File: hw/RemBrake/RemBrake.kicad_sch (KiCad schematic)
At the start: 5 parts, among them J1 Screw_Terminal_01x02, J2 Conn_01x03_MountingPin, J3 Screw_Terminal_01x04

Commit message: schematics update
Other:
- sheet brake_control ports: added none; removed RUNNIG (RED)
- sheet power_switch ports: added RUNNIG (RED); removed none
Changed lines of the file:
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@@
-	(wire
-		(pts
-			(xy 184.15 127) (xy 187.96 127)
-		)
-		(stroke
-			(width 0)
-			(type default)
-		)
-	)
 	(wire
 		(pts
@@
 	(wire
 		(pts
-			(xy 177.8 106.68) (xy 184.15 106.68)
+			(xy 205.74 76.2) (xy 205.74 95.25)
 		)
 		(stroke
@@
 	(wire
 		(pts
-			(xy 184.15 106.68) (xy 184.15 127)
-		)
-		(stroke
-			(width 0)
-			(type default)
-		)
-	)
-	(wire
-		(pts
 			(xy 120.65 101.6) (xy 113.03 101.6)
 		)
@@
 		(pts
 			(xy 113.03 88.9) (xy 109.22 88.9)
+		)
+		(stroke
+			(width 0)
+			(type default)
+		)
+	)
+	(wire
+		(pts
+			(xy 177.8 95.25) (xy 205.74 95.25)
 		)
 		(stroke
@@
 			)
 		)
+		(pin "RUNNIG (RED)" input
+			(at 205.74 76.2 270)
+			(effects
+				(font
+					(size 1.27 1.27)
+				)
+				(justify left)
+			)
+		)
 		(instances
 			(project "RemBrake"
@@
 			)
 		)
-		(pin "RUNNIG (RED)" input
-			(at 187.96 127 180)
-			(effects
-				(font
-					(size 1.27 1.27)
-				)
-				(justify left)
-			)
-		)
 		(instances
 			(project "RemBrake"
@@
 		)
 		(pin "LED RED" input
-			(at 177.8 106.68 0)
-			(effects
-				(font
+			(at 177.8 95.25 0)
+			(effects
+				(font

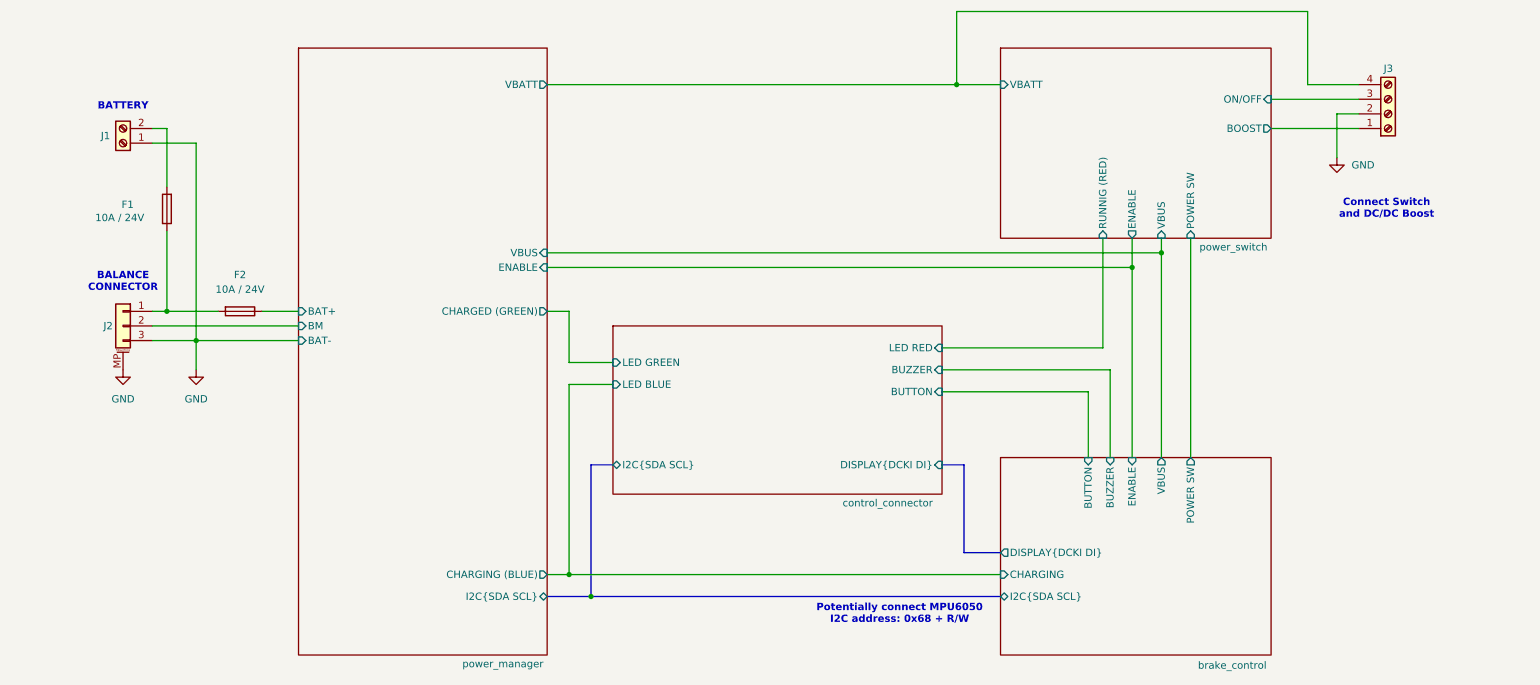
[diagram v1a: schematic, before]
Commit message: finished todos - prepared for routing
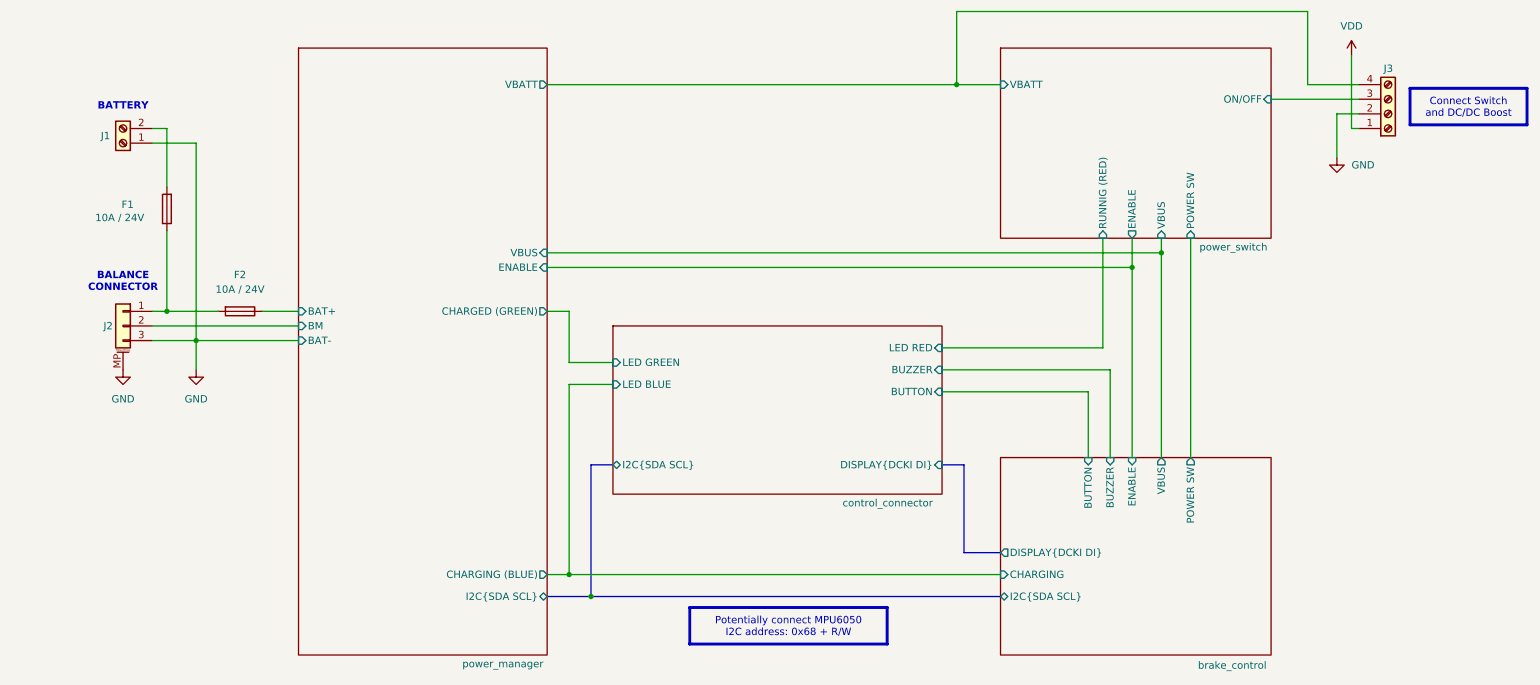
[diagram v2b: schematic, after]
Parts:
- F1, F2: Purchase https://cz.farnell.com/multicomp-pro/mp005472/fuse-fast-act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 -> (none)
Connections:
- net power_switch/BOOST renamed VDD
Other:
- sheet power_switch ports: added none; removed BOOST
- note removed: "Connect Switch and DC/DC Boost"
- note removed: "Potentially connect MPU6050 I2C address: 0x68 + R/W"
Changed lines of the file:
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@@
 		(members "SDA" "SCL")
-	)
-	(text "Potentially connect MPU6050\nI2C address: 0x68 + R/W"
-		(exclude_from_sim no)
-		(at 170.434 141.478 0)
-		(effects
-			(font
-				(size 1.27 1.27)
-				(thickness 0.254)
-				(bold yes)
-			)
-		)
 	)
 	(text "BATTERY"
@@
 		)
 	)
-	(text "Connect Switch\nand DC/DC Boost"
-		(exclude_from_sim no)
-		(at 255.016 71.12 0)
+	(text_box "Potentially connect MPU6050\nI2C address: 0x68 + R/W"
+		(exclude_from_sim no)
+		(at 133.985 140.335 0)
+		(size 34.29 6.35)
+		(margins 0.9525 0.9525 0.9525 0.9525)
+		(stroke
+			(width 0.508)
+			(type solid)
+			(color 128 63 0 1)
+		)
+		(fill
+			(type color)
+			(color 255 255 153 1)
+		)
 		(effects
 			(font
 				(size 1.27 1.27)
-				(thickness 0.254)
-				(bold yes)
+			)
+		)
+	)
+	(text_box "Connect Switch\nand DC/DC Boost"
+		(exclude_from_sim no)
+		(at 259.08 50.165 0)
+		(size 20.32 6.35)
+		(margins 0.9525 0.9525 0.9525 0.9525)
+		(stroke
+			(width 0.508)
+			(type solid)
+			(color 128 63 0 1)
+		)
+		(fill
+			(type color)
+			(color 255 255 153 1)
+		)
+		(effects
+			(font
+				(size 1.27 1.27)
 			)
 		)
@@
 	(wire
 		(pts
+			(xy 250.19 57.15) (xy 248.92 57.15)
+		)
+		(stroke
+			(width 0)
+			(type default)
+		)
+	)
+	(wire
+		(pts
 			(xy 220.98 76.2) (xy 220.98 114.3)
 		)
@@
 		)
 	)
-	(wire
-		(pts
-			(xy 234.95 57.15) (xy 250.19 57.15)
-		)
-		(stroke
-			(width 0)
-			(type default)
-		)
-	)
 	(bus
 		(pts
@@
 		(pts
 			(xy 120.65 101.6) (xy 113.03 101.6)
+		)
+		(stroke
+			(width 0)
+			(type default)
+		)
+	)
+	(wire
+		(pts
+			(xy 248.92 44.45) (xy 248.92 57.15)
 		)
 		(stroke
@@
 			)
 		)
-		(property "Description" "MP005472"
+		(property "Description" "Fuse"
 			(at 55.88 88.9 0)
-			(hide yes)
-			(effects
-				(font
-					(size 1.27 1.27)
-				)
-			)
-		)
-		(property "Purchase" "https://cz.farnell.com/multicomp-pro/mp005472/fuse-fast-acting-10a-24vdc-1206/dp/3564732"
-			(at 55.88 88.9 90)
 			(hide yes)
 			(effects
@@
 			)
 		)
-		(property "Description" "MP005472"
+		(property "Description" "Fuse"
 			(at 43.18 71.12 0)
-			(hide yes)
-			(effects
-				(font
-					(size 1.27 1.27)
-				)
-			)
-		)
-		(property "Purchase" "https://cz.farnell.com/multicomp-pro/mp005472/fuse-fast-acting-10a-24vdc-1206/dp/3564732"
-			(at 43.18 71.12 90)
 			(hide yes)
 			(effects
@@
 	)
 	(symbol
+		(lib_id "power:VDD")
+		(at 248.92 44.45 0)
+		(unit 1)
+		(exclude_from_sim no)
+		(in_bom yes)
+		(on_board yes)
+		(dnp no)
+		(fields_autoplaced yes)
+		(property "Reference" "#PWR04"
+			(at 248.92 48.26 0)
+			(hide yes)
+			(effects
+				(font
+					(size 1.27 1.27)
+				)
+			)
+		)
+		(property "Value" "VDD"
+			(at 248.92 39.37 0)
+			(effects
+				(font
+					(size 1.27 1.27)
+				)
+			)
+		)
+		(property "Footprint" ""
+			(at 248.92 44.45 0)
+			(hide yes)
+			(effects
+				(font
+					(size 1.27 1.27)
+				)
+			)
+		)
+		(property "Datasheet" ""
+			(at 248.92 44.45 0)
+			(hide yes)
+			(effects
+				(font
+					(size 1.27 1.27)
+				)
+			)
+		)
+		(property "Description" "Power symbol creates a global label with name \"VDD\""
+			(at 248.92 44.45 0)
+			(hide yes)
+			(effects
+				(font
+					(size 1.27 1.27)
+				)
+			)
+		)
+		(pin "1"
+		)
+		(instances
+			(project "RemBrake"
+				(path "/e6d4ae5b-c9d7-4cbe-b288-c929fdf55a75"
+					(reference "#PWR04")
+					(unit 1)
+				)
+			)
+		)
+	)
+	(symbol
 		(lib_id "power:GND")
 		(at 35.56 99.06 0)
@@
 			)
 		)
-		(pin "BOOST" output
-			(at 234.95 57.15 0)
-			(effects
-				(font
-					(size 1.27 1.27)
-				)
-				(justify right)
-			)
-		)

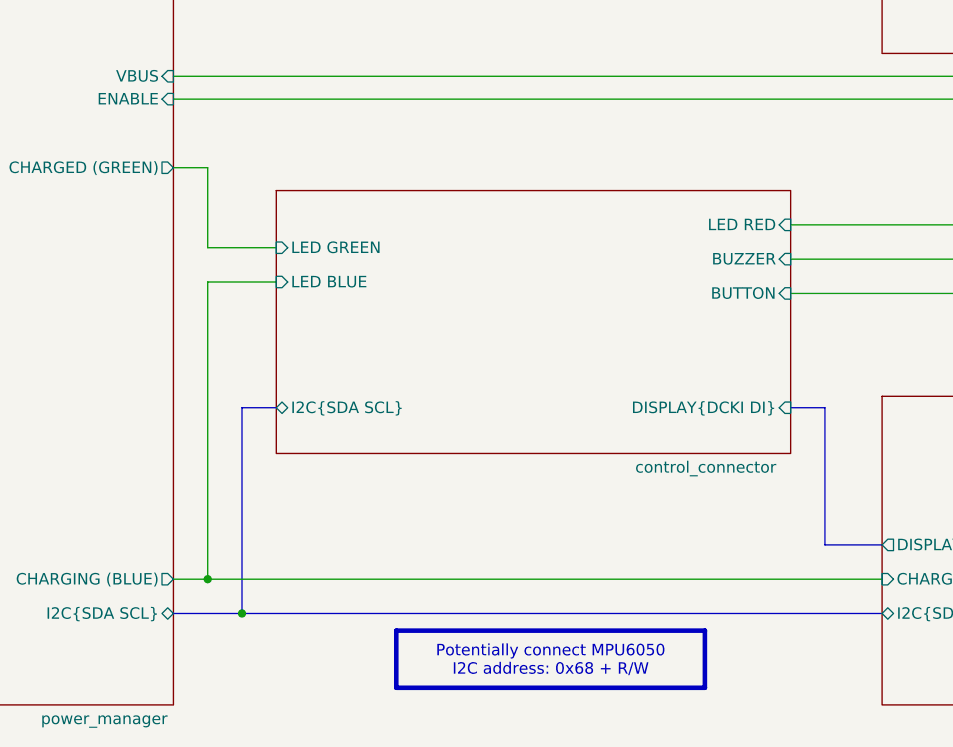
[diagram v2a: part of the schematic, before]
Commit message: updated schematics and pcb - smd transistor was not connected to resistor to limit current through buzzer
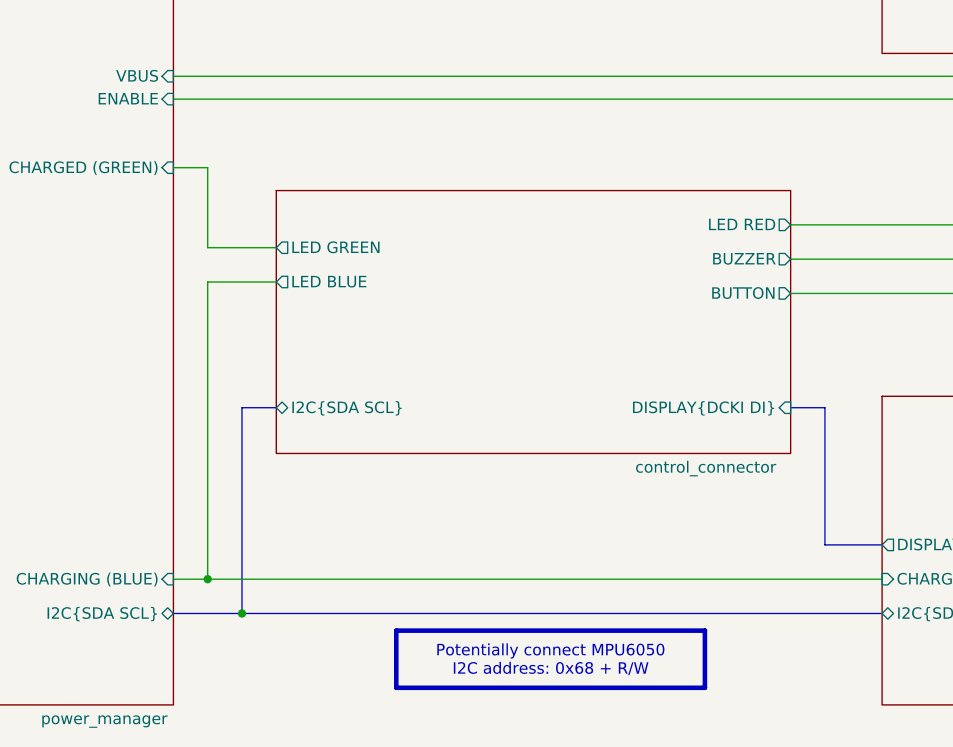
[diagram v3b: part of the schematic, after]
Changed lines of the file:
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@@
 			)
 		)
-		(pin "CHARGING (BLUE)" output
+		(pin "CHARGING (BLUE)" input
 			(at 109.22 134.62 0)
 			(effects
@@
 			)
 		)
-		(pin "CHARGED (GREEN)" output
+		(pin "CHARGED (GREEN)" input
 			(at 109.22 88.9 0)
 			(effects
@@
 			)
 		)
-		(pin "LED GREEN" input
+		(pin "LED GREEN" output
 			(at 120.65 97.79 180)
 			(effects
@@
 			)
 		)
-		(pin "LED RED" input
+		(pin "LED RED" output
 			(at 177.8 95.25 0)
 			(effects
@@
 			)
 		)
-		(pin "LED BLUE" input
+		(pin "LED BLUE" output
 			(at 120.65 101.6 180)
 			(effects
@@
 			)
 		)
-		(pin "BUTTON" input
+		(pin "BUTTON" output
 			(at 177.8 102.87 0)
 			(effects
@@
 			)
 		)
-		(pin "BUZZER" input
+		(pin "BUZZER" output
 			(at 177.8 99.06 0)
 			(effects

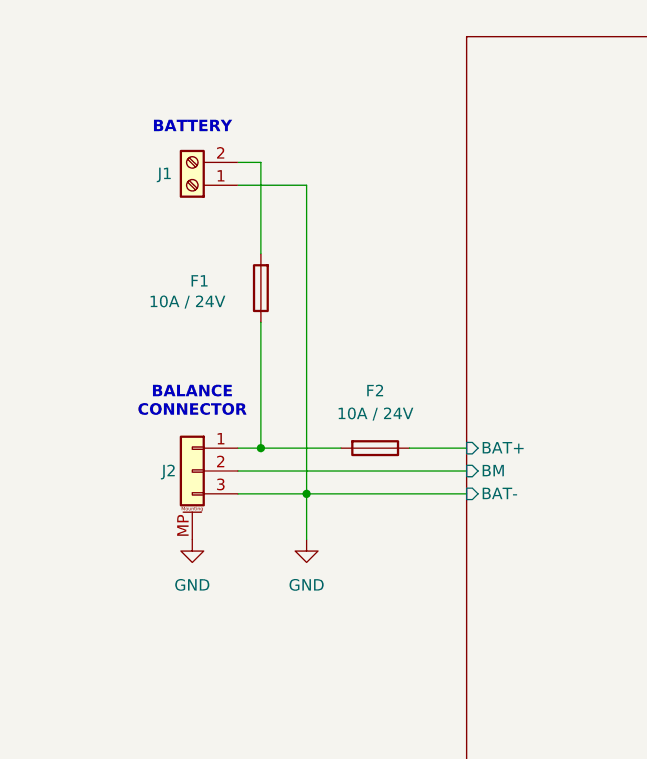
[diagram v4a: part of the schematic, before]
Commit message: updated pcb and added Notes about possible faults
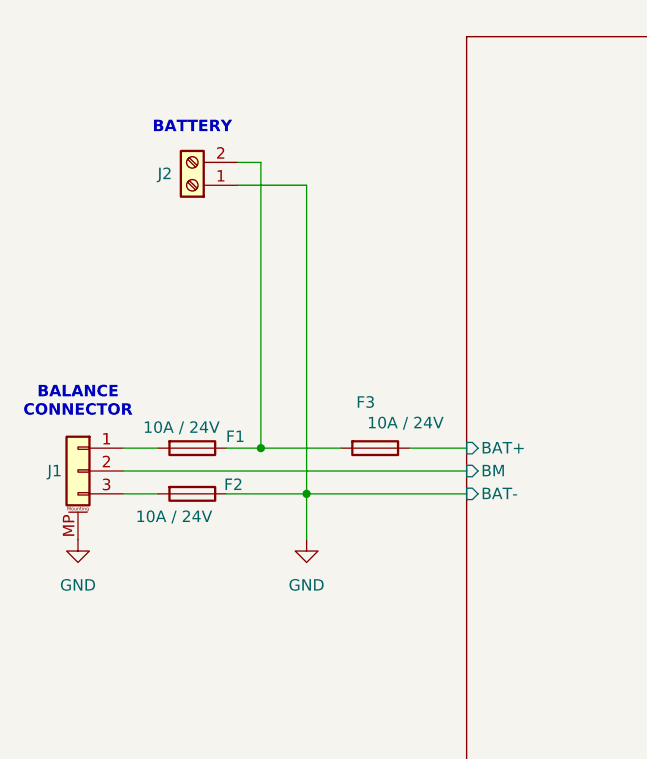
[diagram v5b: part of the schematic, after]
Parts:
- added F3: 10A / 24V, Fuse:Fuse_1206_3216Metric_Pad1.42x1.75mm_HandSolder, symbol Device:Fuse
- renumbered J2 to J1, J1 to J2
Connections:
- net GND: now also F2.1; no longer J1.3 (Pin_3)
- net power_manager/BAT+: now also F3.1; no longer F2.1
- net at J2.2 (Pin_2): now also F1.1, F3.2; no longer F1.2
- new net: F2.2, J1.3 (Pin_3)
- new net: F1.2, J1.1 (Pin_1)
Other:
- moved on the sheet: F1, F2, J1

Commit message: added protection diode at the power input
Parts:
- removed F3: 10A / 24V, Fuse:Fuse_1206_3216Metric_Pad1.42x1.75mm_HandSolder, symbol Device:Fuse
- added D1: MBR0520, Diode_SMD:D_SMA, symbol Device:D_Schottky
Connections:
- net power_manager/BAT+: now also D1.1 (K)
- net at F1.1, J2.2 (Pin_2): now also D1.2 (A)
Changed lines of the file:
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@@
 (kicad_sch
-	(version 20250513)
+	(version 20250610)
 	(generator "eeschema")
 	(generator_version "9.99")
@@
 	)
 	(symbol
-		(lib_id "Device:Fuse")
-		(at 55.88 88.9 270)
-		(unit 1)
-		(exclude_from_sim no)
-		(in_bom yes)
-		(on_board yes)
-		(dnp no)
-		(property "Reference" "F3"
-			(at 55.88 83.82 90)
-			(effects
-				(font
-					(size 1.27 1.27)
-				)
-				(justify right)
-			)
-		)
-		(property "Value" "10A / 24V"
-			(at 63.5 86.106 90)
-			(effects
-				(font
-					(size 1.27 1.27)
-				)
-				(justify right)
-			)
-		)
-		(property "Footprint" "Fuse:Fuse_1206_3216Metric_Pad1.42x1.75mm_HandSolder"
-			(at 55.88 87.122 90)
-			(hide yes)
-			(effects
-				(font
-					(size 1.27 1.27)
-				)
-			)
-		)
-		(property "Datasheet" ""
-			(at 55.88 88.9 0)
-			(hide yes)
-			(effects
-				(font
-					(size 1.27 1.27)
-				)
-			)
-		)
-		(property "Description" "Fuse"
-			(at 55.88 88.9 0)
-			(hide yes)
-			(effects
-				(font
-					(size 1.27 1.27)
-				)
-			)
-		)
-		(property "Purchase" ""
-			(at 55.88 88.9 0)
-			(hide yes)
-			(effects
-				(font
-					(size 1.27 1.27)
-				)
-			)
-		)
-		(pin "1"
-		)
-		(pin "2"
-		)
-		(instances
-			(project "RemBrake"
-				(path "/e6d4ae5b-c9d7-4cbe-b288-c929fdf55a75"
-					(reference "F3")
-					(unit 1)
-				)
-			)
-		)
-	)
-	(symbol
 		(lib_id "Connector:Screw_Terminal_01x02")
 		(at 35.56 59.69 180)
@@
 				(path "/e6d4ae5b-c9d7-4cbe-b288-c929fdf55a75"
 					(reference "J2")
+					(unit 1)
+				)
+			)
+		)
+	)
+	(symbol
+		(lib_id "Device:D_Schottky")
+		(at 55.88 88.9 180)
+		(unit 1)
+		(exclude_from_sim no)
+		(in_bom yes)
+		(on_board yes)
+		(dnp no)
+		(property "Reference" "D1"
+			(at 55.88 86.36 0)
+			(effects
+				(font
+					(size 1.27 1.27)
+				)
+			)
+		)
+		(property "Value" "MBR0520"
+			(at 56.1975 92.71 0)
+			(hide yes)
+			(effects
+				(font
+					(size 1.27 1.27)
+				)
+			)
+		)
+		(property "Footprint" "Diode_SMD:D_SMA"
+			(at 55.88 88.9 0)
+			(hide yes)
+			(effects
+				(font
+					(size 1.27 1.27)
+				)
+			)
+		)
+		(property "Datasheet" ""
+			(at 55.88 88.9 0)
+			(hide yes)
+			(effects
+				(font
+					(size 1.27 1.27)
+				)
+			)
+		)
+		(property "Description" "Schottky diode"
+			(at 55.88 88.9 0)
+			(hide yes)
+			(effects
+				(font
+					(size 1.27 1.27)
+				)
+			)
+		)
+		(property "Purchase" ""
+			(at 55.88 88.9 0)
+			(hide yes)
+			(effects
+				(font
+					(size 1.27 1.27)
+				)
+			)
+		)
+		(pin "1"
+		)
+		(pin "2"
+		)
+		(instances
+			(project "RemBrake"
+				(path "/e6d4ae5b-c9d7-4cbe-b288-c929fdf55a75"
+					(reference "D1")
 					(unit 1)
 				)
@@
 		)
 		(fill
-			(color 0 0 0 0.0000)
+			(color 0 0 0 0)
 		)
 		(property "Sheetname" "power_switch"
@@
 		)
 		(fill
-			(color 0 0 0 0.0000)
+			(color 0 0 0 0)
 		)
 		(property "Sheetname" "brake_control"
@@
 		)
 		(fill
-			(color 0 0 0 0.0000)
+			(color 0 0 0 0)
 		)
 		(property "Sheetname" "power_manager"
@@
 		)
 		(fill
-			(color 0 0 0 0.0000)
+			(color 0 0 0 0)
 		)
 		(property "Sheetname" "control_connector"

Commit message: updated BOM list and reduced number of different capacitors and resistors
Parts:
- D1: value MBR0520 -> SS1200
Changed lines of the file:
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@@
 			)
 		)
-		(property "Value" "MBR0520"
+		(property "Value" "SS1200"
 			(at 56.1975 92.71 0)
 			(hide yes)
